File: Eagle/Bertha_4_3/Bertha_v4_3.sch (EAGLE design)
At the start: 115 parts, among them CON1 JACK_DC_BARREL, IC1 MCP1703DB, J1 RJ12RIGHTANGLE-I2C, J2 RJ12RIGHTANGLE-I2C, J7 22--02, Q1 BSP75, Q2 BSP75, Q3 BSP75, Q4 BSP75, Q5 BSP75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

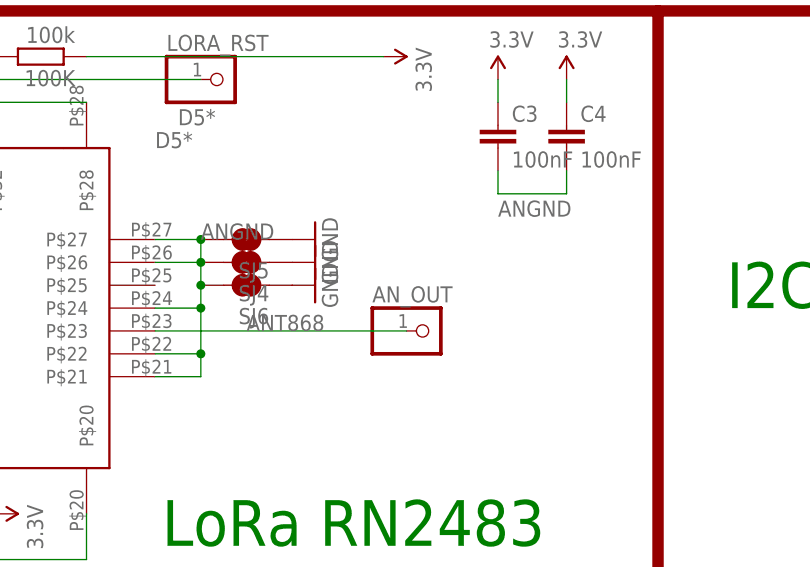
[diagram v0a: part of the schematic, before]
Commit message: Added SMA LoRa antenna for 4.3 ref #18, same needs to be done for the pH board
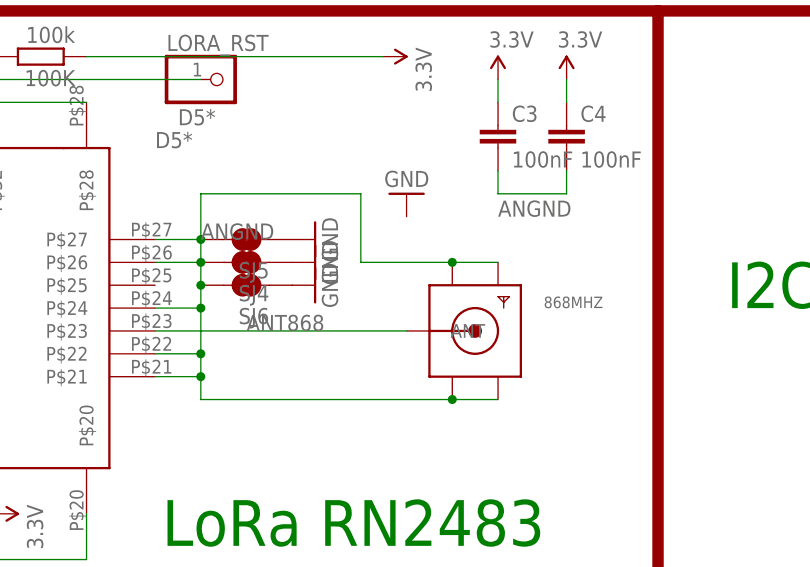
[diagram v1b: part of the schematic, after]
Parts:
- removed AN_OUT: (no value), Headerlibrary:PINHD-1X1
- added 868MHZ: (no value), sma_end_launch:SMACONNECTOR_EDGE
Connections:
- net ANGND: now also 868MHZ.GND1, 868MHZ.GND2, 868MHZ.GND3, 868MHZ.GND4
- net ANT868: now also 868MHZ.ANT; no longer AN_OUT.1
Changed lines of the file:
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@@
 <?xml version="1.0" encoding="utf-8"?>
 <!DOCTYPE eagle SYSTEM "eagle.dtd">
-<eagle version="6.5.0">
+<eagle version="7.6.0">
 <drawing>
 <settings>
@@
 <part name="P+25" library="SparkFun" deviceset="3.3V" device=""/>
 <part name="P+26" library="SparkFun" deviceset="3.3V" device=""/>
-<part name="AN_OUT" library="Headerlibrary" deviceset="PINHD-1X1" device=""/>
 <part name="RXT" library="rcl" deviceset="R-EU_" device="R0805" value="1M"/>
 <part name="C2" library="rcl" deviceset="C-EU" device="C1206" value="100nF"/>
@@
 <part name="P+42" library="SparkFun" deviceset="3.3V" device=""/>
 <part name="P+43" library="supply1" deviceset="+12V" device=""/>
+<part name="868MHZ" library="sma_end_launch" deviceset="SMACONNECTOR" device="_EDGE"/>
+<part name="GND9" library="supply1" deviceset="GND" device=""/>
 </parts>
 <sheets>
@@
 <instance part="P+25" gate="G$1" x="289.56" y="281.94"/>
 <instance part="P+26" gate="G$1" x="226.06" y="233.68" rot="R270"/>
-<instance part="AN_OUT" gate="G$1" x="274.32" y="254"/>
 <instance part="RXT" gate="G$1" x="271.78" y="132.08" rot="MR90"/>
 <instance part="C2" gate="G$1" x="167.64" y="241.3"/>
@@
 <instance part="P+42" gate="G$1" x="436.88" y="45.72"/>
 <instance part="P+43" gate="1" x="165.1" y="246.38"/>
+<instance part="868MHZ" gate="G$1" x="279.4" y="254"/>
+<instance part="GND9" gate="1" x="271.78" y="269.24" rot="R180"/>
 </instances>
 <busses>
@@
 <wire x1="271.78" y1="254" x2="243.84" y2="254" width="0.1524" layer="91"/>
 <label x="254" y="254" size="1.778" layer="95"/>
-<pinref part="AN_OUT" gate="G$1" pin="1"/>
+<pinref part="868MHZ" gate="G$1" pin="ANT"/>
 </segment>
 </net>
@@
 <pinref part="SJ6" gate="G$1" pin="2"/>
 <junction x="248.92" y="259.08"/>
+<pinref part="868MHZ" gate="G$1" pin="GND4"/>
+<pinref part="868MHZ" gate="G$1" pin="GND3"/>
+<wire x1="281.94" y1="246.38" x2="276.86" y2="246.38" width="0.1524" layer="91"/>
+<wire x1="276.86" y1="246.38" x2="248.92" y2="246.38" width="0.1524" layer="91"/>
+<wire x1="248.92" y1="246.38" x2="248.92" y2="248.92" width="0.1524" layer="91"/>
+<junction x="276.86" y="246.38"/>
+<junction x="248.92" y="248.92"/>
+<pinref part="868MHZ" gate="G$1" pin="GND2"/>
+<pinref part="868MHZ" gate="G$1" pin="GND1"/>
+<wire x1="281.94" y1="261.62" x2="276.86" y2="261.62" width="0.1524" layer="91"/>
+<wire x1="276.86" y1="261.62" x2="266.7" y2="261.62" width="0.1524" layer="91"/>
+<wire x1="266.7" y1="261.62" x2="266.7" y2="269.24" width="0.1524" layer="91"/>
+<junction x="276.86" y="261.62"/>
+<wire x1="266.7" y1="269.24" x2="248.92" y2="269.24" width="0.1524" layer="91"/>
+<wire x1="248.92" y1="269.24" x2="248.92" y2="264.16" width="0.1524" layer="91"/>
 </segment>
 <segment>
